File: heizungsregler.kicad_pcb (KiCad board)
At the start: 2 copper layers, 65 x 30 mm, 46 parts, among them J101 RPi_GPIO, J201 SI-52008-F, U201 ENC28J60x-SS, U202 TPS54231, Y201 Crystal

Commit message: Schaltplan weitergemacht, Footprints zugeordnet
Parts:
- removed C201, C202: 22P, Capacitor_SMD:C_0603_1608Metric
- removed C203, C204, C205, C206, C208, C212: 100N, Capacitor_SMD:C_0603_1608Metric
- removed C207, C213, C215: 10U, Capacitor_SMD:C_1210_3225Metric
- removed C209: 8N2, Capacitor_SMD:C_0603_1608Metric
- removed C210: 82P, Capacitor_SMD:C_0603_1608Metric
- removed C211: 4N3, Capacitor_SMD:C_0603_1608Metric
- removed C214: 47U, Capacitor_SMD:C_1210_3225Metric
- removed D201: D_Schottky, Diode_SMD:D_SOD-123
- removed FB201: Ferrite_Bead, Inductor_SMD:L_0603_1608Metric
- removed J101: RPi_GPIO, Connector_Samtec_HLE_THT:Samtec_HLE-120-02-xx-DV-TE_2x20_P2.54mm_Horizontal
- removed J201: SI-52008-F, kicadlibs:RJ45_BEL_STEWART_SI-52008-F
- removed L201: 22U, Inductor_SMD:L_Bourns_SRN6045TA
- removed R201, R202, R203, R204, R205, R206, R211: 0R00, Resistor_SMD:R_0603_1608Metric
- removed R207, R208, R209, R210: 49R9, Resistor_SMD:R_0603_1608Metric
- removed R212, R213: 220R, Resistor_SMD:R_0603_1608Metric
- removed R214: 2K32, Resistor_SMD:R_0603_1608Metric
- removed R215: 19K6, Resistor_SMD:R_0603_1608Metric
- removed R216: 18K7, Resistor_SMD:R_0603_1608Metric
- removed R217: 169K, Resistor_SMD:R_0603_1608Metric
- removed R218: 10K2, Resistor_SMD:R_0603_1608Metric
- removed R219: 1K96, Resistor_SMD:R_0603_1608Metric
- removed U201: ENC28J60x-SS, Package_SO:SSOP-28_5.3x10.2mm_P0.65mm
- removed U202: TPS54231, Package_SO:SOIC-8_3.9x4.9mm_P1.27mm
- removed Y201: Crystal, Crystal:Crystal_SMD_HC49-SD
- added C301: 22U, Capacitor_SMD:C_1210_3225Metric, F.Cu at (127.6, 38.6)
- added C302: 330P, Capacitor_SMD:C_0603_1608Metric, F.Cu at (135.8, 41.3)
- added C303: 47U, Capacitor_SMD:C_1210_3225Metric, F.Cu at (122.5, 44.2)
- added C304: 47U, Capacitor_SMD:C_1210_3225Metric, F.Cu at (133.4, 32.4)
- added D301: D_Schottky, Diode_SMD:D_SOD-123, F.Cu at (115.0, 44.7)
- added F301: Fuse, Fuse:Fuse_1812_4532Metric, F.Cu at (128.1, 32.8)
- added J102: Conn_01x03_Male, Connector_PinHeader_2.54mm:PinHeader_1x03_P2.54mm_Vertical, F.Cu at (89.2, 32.6)
- added J103: Conn_01x10_Male, Connector_PinHeader_2.54mm:PinHeader_1x10_P2.54mm_Vertical, F.Cu at (85.6, 32.6)
- added J301: Conn_01x02_Male, Connector_PinHeader_2.54mm:PinHeader_1x02_P2.54mm_Vertical, F.Cu at (123.3, 32.6)
- added L301: 150U, Inductor_SMD:L_Bourns-SRN4018, F.Cu at (122.7, 40.3)
- added L302: 1U, Inductor_SMD:L_1206_3216Metric, F.Cu at (127.5, 35.9)
- added Q301: BC847, Package_TO_SOT_SMD:SOT-23, F.Cu at (137.4, 32.6)
- added Q302: BC847, Package_TO_SOT_SMD:SOT-23, F.Cu at (132.8, 35.8)
- added Q303: BCP51, Package_TO_SOT_SMD:SOT-223, F.Cu at (117.1, 34.4)
- added R101: R, Resistor_SMD:R_0603_1608Metric, F.Cu at (57.2, 59.6)
- added R102: R, Resistor_SMD:R_0603_1608Metric, F.Cu at (85.3, 58.1)
- added R301: 0R00, Resistor_SMD:R_0603_1608Metric, F.Cu at (135.8, 39.8)
- added R302: 0R00, Resistor_SMD:R_0603_1608Metric, F.Cu at (129.3, 44.0)
- added R303: 1K, Resistor_SMD:R_0603_1608Metric, F.Cu at (132.8, 39.8)
- added R304: 1K, Resistor_SMD:R_0603_1608Metric, F.Cu at (136.1, 36.6)
- added R305: 0R47, Resistor_SMD:R_0603_1608Metric, F.Cu at (134.4, 38.3)
- added R306: 180, Resistor_SMD:R_0603_1608Metric, F.Cu at (126.3, 44.9)
- added R307: 4k7, Resistor_SMD:R_0603_1608Metric, F.Cu at (129.3, 42.5)
- added R308: 39K, Resistor_SMD:R_0603_1608Metric, F.Cu at (136.1, 35.1)
- added R309: 22K, Resistor_SMD:R_0603_1608Metric, F.Cu at (129.8, 41.0)
- added R310: 100K, Resistor_SMD:R_0603_1608Metric, F.Cu at (131.4, 38.3)
- added R311: 33K, Resistor_SMD:R_0603_1608Metric, F.Cu at (126.3, 43.4)
- added R312: 3K3, Resistor_SMD:R_0603_1608Metric, F.Cu at (126.8, 41.0)
- added R313: 22K, Resistor_SMD:R_0603_1608Metric, F.Cu at (132.8, 41.3)
- added R314: 220K, Resistor_SMD:R_0603_1608Metric, F.Cu at (137.4, 38.1)
- added R315: 82R, Resistor_SMD:R_0603_1608Metric, F.Cu at (132.3, 42.8)
- added U101: oled_0.96, kicadlibs:oled_0.96, F.Cu at (129.0, 114.1)
- added U301: MC34063AD, Package_SO:SOIC-8_3.9x4.9mm_P1.27mm, F.Cu at (116.4, 40.8)

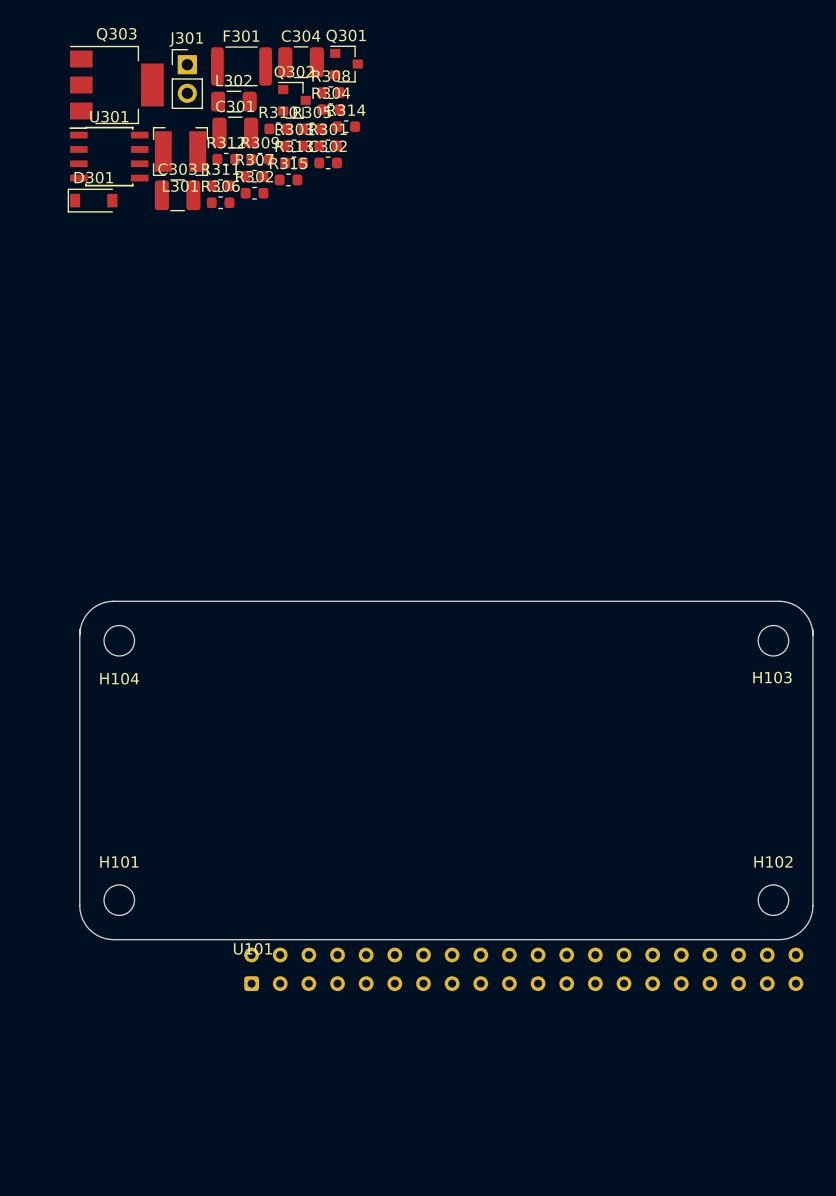
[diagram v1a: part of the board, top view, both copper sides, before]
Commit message: Platzierung begonnen, Signalnamen ENC korrigiert
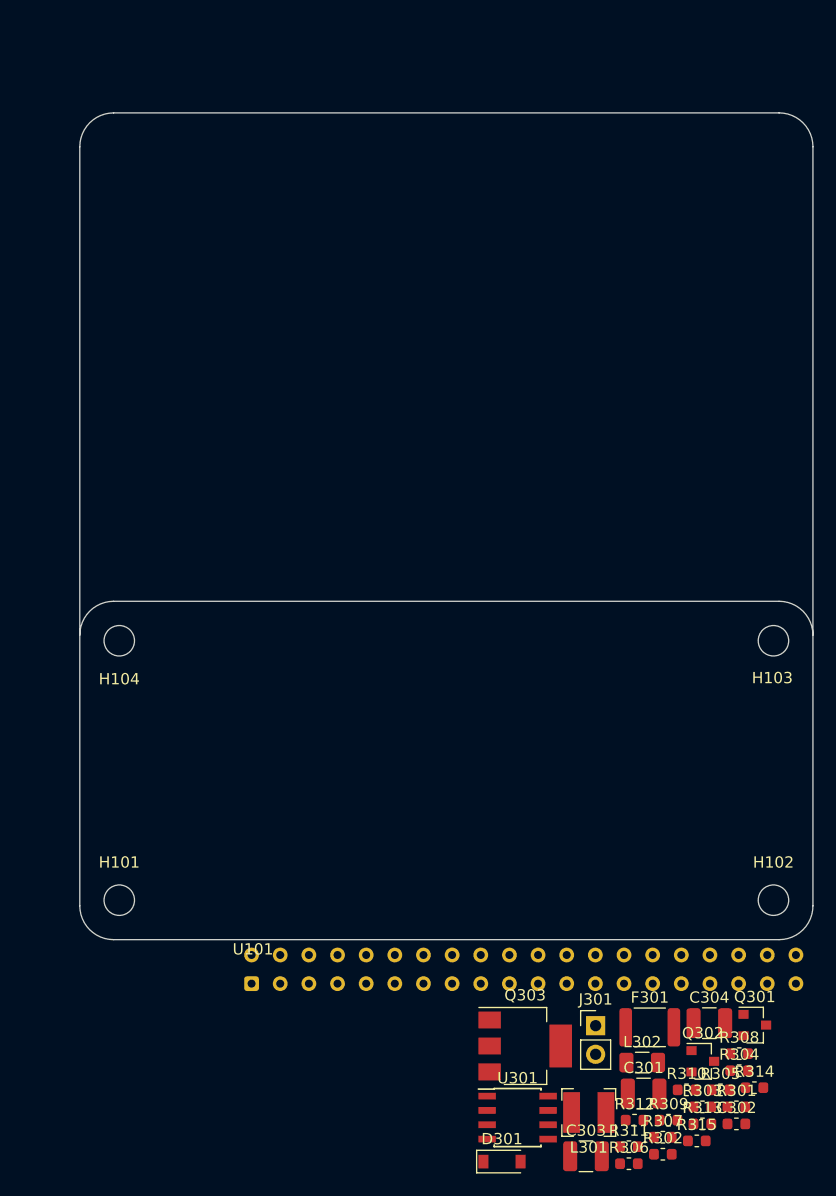
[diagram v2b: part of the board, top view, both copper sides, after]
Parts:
- moved C304 92.6 mm to (169.6, 117.6)
- moved F301 92.6 mm to (164.3, 118.0)
- moved Q301 92.6 mm to (173.6, 117.8)
- moved R301 92.6 mm to (172.0, 125.0)
- moved R308 92.6 mm to (172.3, 120.3)
- moved R311 92.6 mm to (162.5, 128.6)
- moved R314 92.6 mm to (173.6, 123.3)
- moved C302 92.6 mm to (172.0, 126.5)
- moved C303 92.6 mm to (158.7, 129.4)
- moved D301 92.6 mm to (151.2, 129.9)
- moved R304 92.6 mm to (172.3, 121.8)
- moved R306 92.6 mm to (162.5, 130.1)
- moved R312 92.6 mm to (163.0, 126.2)
- moved R315 92.6 mm to (168.5, 128.0)
- moved J301 92.6 mm to (159.5, 117.8)
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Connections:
- net /EN_#CS renamed /ENC_#CS
- net /EN_#INT renamed /ENC_#INT
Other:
- board size 65 x 30 mm -> 65 x 73.3 mm

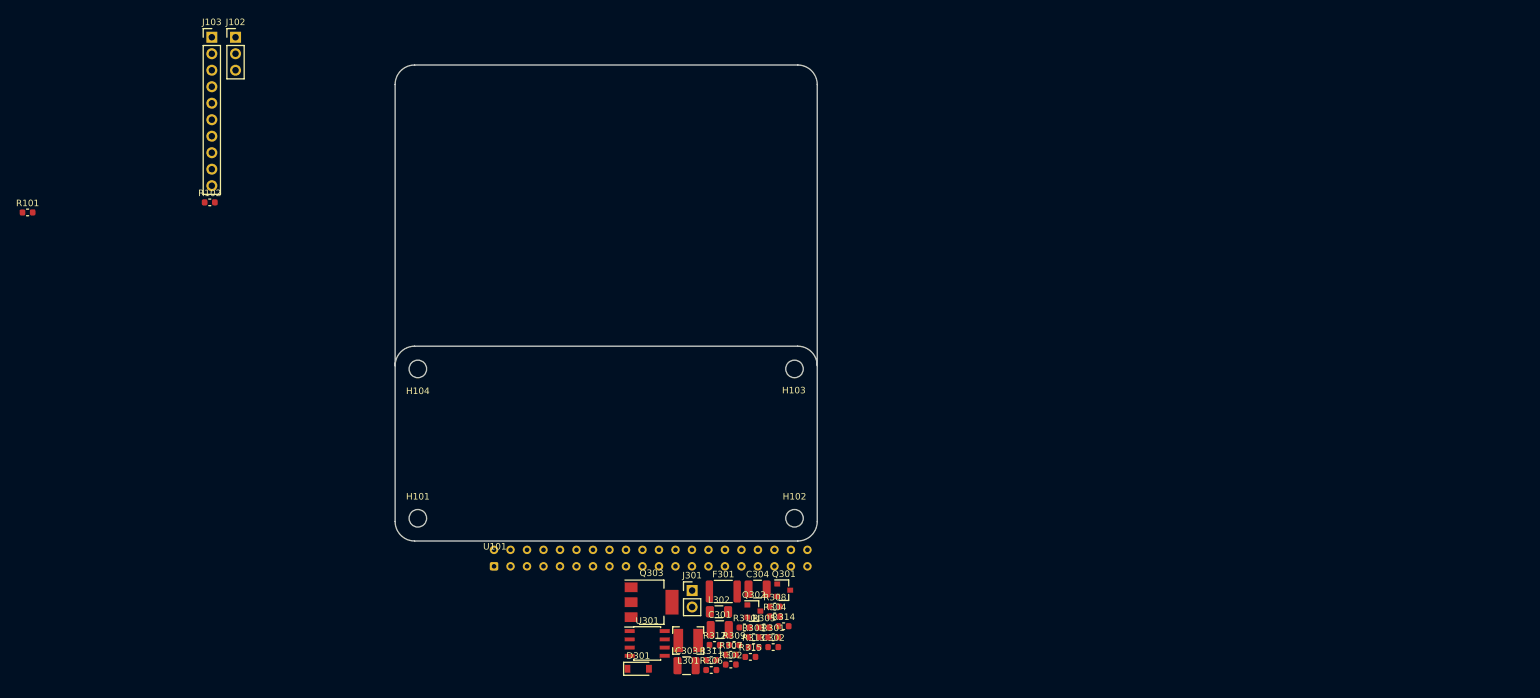
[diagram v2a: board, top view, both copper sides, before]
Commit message: ENC28J60 platziert und geroutet
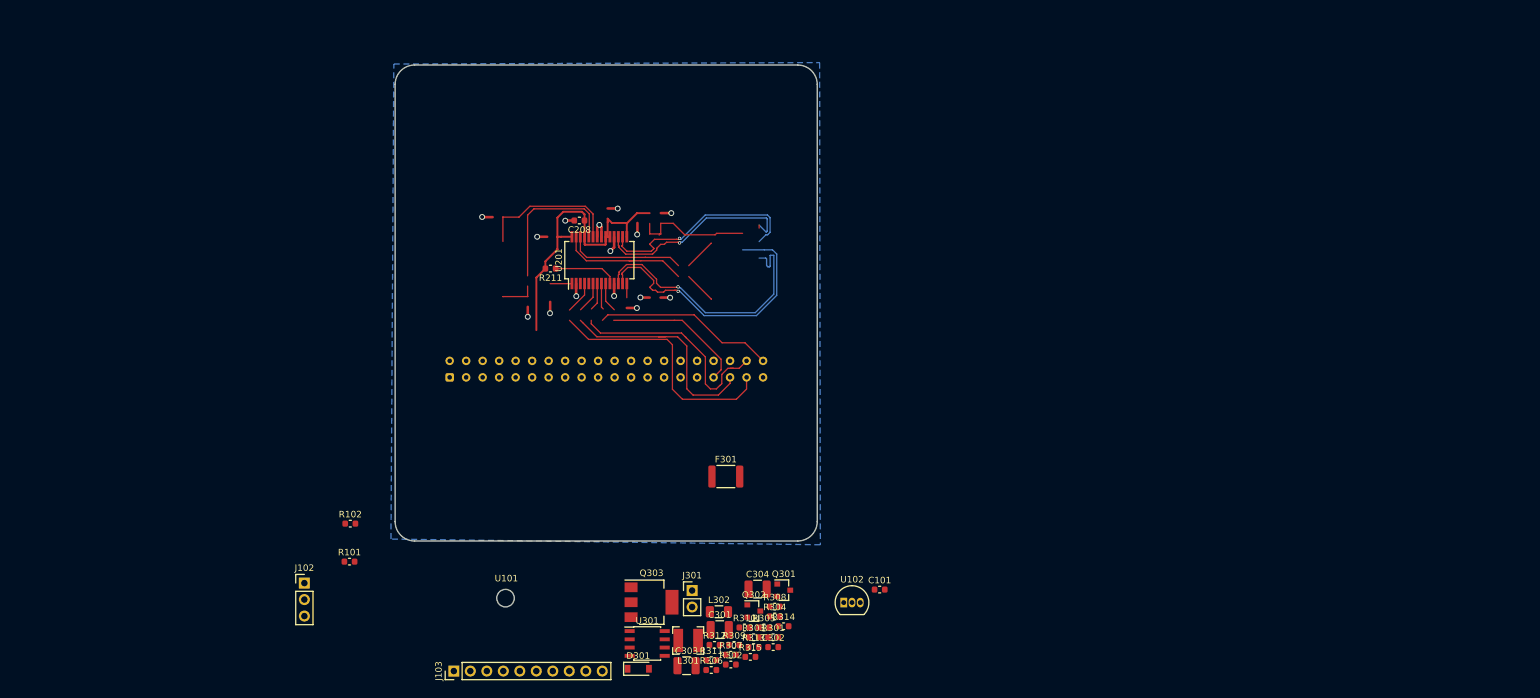
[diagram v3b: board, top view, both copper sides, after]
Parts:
- removed H101, H102, H103, H104: MountingHole, MountingHole:MountingHole_2.7mm_M2.5_DIN965
- added C101: C, Capacitor_SMD:C_0603_1608Metric, F.Cu at (188.4, 117.7)
- added C208: 100N, Capacitor_SMD:C_0603_1608Metric, F.Cu at (142.2, 60.9)
- added J101: RPi_GPIO, Connector_Samtec_HLE_THT:Samtec_HLE-120-02-xx-DV-TE_2x20_P2.54mm_Horizontal, B.Cu at (122.2, 85.0)
- added R211: 0R00, Resistor_SMD:R_0603_1608Metric, F.Cu at (137.7, 68.2)
- added U102: DS18B20, Package_TO_SOT_THT:TO-92_Inline, F.Cu at (182.9, 119.7)
- added U201: ENC28J60x-SS, Package_SO:SSOP-28_5.3x10.2mm_P0.65mm, F.Cu at (145.2, 67.0)
- F301: value Fuse -> Fuse 2A
- moved J103 104.5 mm to (122.8, 130.2), turned to 90 degrees
- moved J102 84.7 mm to (99.8, 116.7)
- moved R101 73.1 mm to (106.8, 113.4)
- moved R102 54.0 mm to (106.9, 107.5)
- moved F301 17.7 mm to (164.7, 100.3)
- moved U101 5.21 mm to (130.8, 119.0)
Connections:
- U101 pad 1: +3V3 -> (no net)
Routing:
- net +3V3: track 0.00 -> 48.0 mm
- net /Ethernet/TPIN+: track 0.00 -> 43.9 mm, vias 0 -> 1
- net /Ethernet/TPIN-: track 0.00 -> 41.9 mm, vias 0 -> 1
- net /ENC_#INT: track 0.00 -> 38.8 mm
- net /ENC_SO: track 0.00 -> 34.4 mm
- net /ENC_SI: track 0.00 -> 34.4 mm
- net /Ethernet/TPOUT-: track 0.00 -> 33.1 mm, vias 0 -> 1
- net /Ethernet/TPOUT+: track 0.00 -> 31.6 mm, vias 0 -> 1
- net /ENC_SCK: track 0.00 -> 28.0 mm
- net GND: track 0.00 -> 27.5 mm, vias 0 -> 15
- net Net-(R206-Pad1): track 0.00 -> 23.1 mm
- net Net-(C201-Pad1): track 0.00 -> 22.3 mm
- net /ENC_#CS: track 0.00 -> 22.3 mm
- net /Ethernet/LED_A: track 0.00 -> 20.0 mm
- net Net-(C203-Pad1): track 0.00 -> 18.7 mm
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- added copper zone on B.Cu, net GND
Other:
- outline, holes or cut-outs redrawn
- net class Default: trace_width 0.25 -> 0.2; via_dia 0.6 -> 0.5; via_drill 0.4 -> 0.3
- net class GND added: clearance 0.2, trace_width 0.4, via_dia 0.9, via_drill 0.6
- net class PWR added: clearance 0.2, trace_width 0.3, via_dia 0.5, via_drill 0.3
- rule trace_min: 0.01 -> 0.2
- rule via_min_size: 0.4 -> 0.5

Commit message: Noch mehr Layout
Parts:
- removed J101: RPi_GPIO, Connector_Samtec_HLE_THT:Samtec_HLE-120-02-xx-DV-TE_2x20_P2.54mm_Horizontal
- removed R102: R, Resistor_SMD:R_0603_1608Metric
- added C201: 22P, Capacitor_SMD:C_0603_1608Metric, F.Cu at (129.7, 57.2)
- added C202: 22P, Capacitor_SMD:C_0603_1608Metric, F.Cu at (134.3, 70.2)
- added C203: 100N, Capacitor_SMD:C_0603_1608Metric, F.Cu at (154.8, 57.3)
- added C204: 100N, Capacitor_SMD:C_0603_1608Metric, F.Cu at (146.9, 57.0)
- added C205: 100N, Capacitor_SMD:C_0603_1608Metric, F.Cu at (138.1, 60.2)
- added C206: 100N, Capacitor_SMD:C_0603_1608Metric, F.Cu at (150.4, 58.1)
- added C207: 10U, Capacitor_SMD:C_1210_3225Metric, F.Cu at (137.7, 68.8)
- added C209: 8N2, Capacitor_SMD:C_0603_1608Metric, F.Cu at (219.9, 47.9)
- added C210: 82P, Capacitor_SMD:C_0603_1608Metric, F.Cu at (204.4, 62.9)
- added C211: 4N3, Capacitor_SMD:C_0603_1608Metric, F.Cu at (214.6, 53.1)
- added C212: 100N, Capacitor_SMD:C_0603_1608Metric, F.Cu at (214.6, 51.6)
- added C213: 10U, Capacitor_SMD:C_1210_3225Metric, F.Cu at (207.7, 53.5)
- added C214: 47U, Capacitor_SMD:C_1210_3225Metric, F.Cu at (198.2, 68.8)
- added C215: 10U, Capacitor_SMD:C_1210_3225Metric, F.Cu at (199.4, 74.6)
- added D201: D_Schottky, Diode_SMD:D_SOD-123, F.Cu at (207.8, 50.7)
- added FB201: Ferrite_Bead, Inductor_SMD:L_0603_1608Metric, F.Cu at (153.1, 57.3)
- added H101: MountingHole, MountingHole:MountingHole_2.7mm_M2.5_DIN965, F.Cu at (117.3, 106.7)
- added H102: MountingHole, MountingHole:MountingHole_2.7mm_M2.5_DIN965, F.Cu at (175.3, 106.7)
- added H103: MountingHole, MountingHole:MountingHole_2.7mm_M2.5_DIN965, F.Cu at (175.3, 83.7)
- added H104: MountingHole, MountingHole:MountingHole_2.7mm_M2.5_DIN965, F.Cu at (117.3, 83.7)
- added L201: 22U, Inductor_SMD:L_Bourns_SRN6045TA, F.Cu at (193.1, 81.7)
- added R201: 0R00, Resistor_SMD:R_0603_1608Metric, F.Cu at (144.1, 72.3)
- added R202: 0R00, Resistor_SMD:R_0603_1608Metric, F.Cu at (142.4, 72.3)
- added R203: 0R00, Resistor_SMD:R_0603_1608Metric, F.Cu at (145.8, 72.3)
- added R204: 0R00, Resistor_SMD:R_0603_1608Metric, F.Cu at (147.5, 72.3)
- added R205: 0R00, Resistor_SMD:R_0603_1608Metric, F.Cu at (140.7, 72.3)
- added R206: 0R00, Resistor_SMD:R_0603_1608Metric, F.Cu at (134.2, 67.0)
- added R207: 49R9, Resistor_SMD:R_0603_1608Metric, F.Cu at (154.8, 60.6)
- added R208: 49R9, Resistor_SMD:R_0603_1608Metric, F.Cu at (153.1, 68.8)
- added R209: 49R9, Resistor_SMD:R_0603_1608Metric, F.Cu at (153.1, 60.5)
- added R210: 49R9, Resistor_SMD:R_0603_1608Metric, F.Cu at (154.7, 68.8)
- added R212: 220R, Resistor_SMD:R_0603_1608Metric, F.Cu at (158.3, 64.6)
- added R213: 220R, Resistor_SMD:R_0603_1608Metric, F.Cu at (158.3, 66.3)
- added R214: 2K32, Resistor_SMD:R_0603_1608Metric, F.Cu at (149.5, 70.4)
- added R215: 19K6, Resistor_SMD:R_0603_1608Metric, F.Cu at (221.5, 46.2)
- added R216: 18K7, Resistor_SMD:R_0603_1608Metric, F.Cu at (217.7, 49.4)
- added R217: 169K, Resistor_SMD:R_0603_1608Metric, F.Cu at (194.3, 70.6)
- added R218: 10K2, Resistor_SMD:R_0603_1608Metric, F.Cu at (214.7, 50.1)
- added R219: 1K96, Resistor_SMD:R_0603_1608Metric, F.Cu at (209.9, 55.9)
- added U202: TPS54231, Package_SO:SOIC-8_3.9x4.9mm_P1.27mm, F.Cu at (211.6, 46.6)
- added Y201: Crystal, Crystal:Crystal_SMD_HC49-SD, F.Cu at (130.4, 65.2)
- moved U102 83.9 mm to (117.1, 67.6), turned to 270 degrees
- moved C101 83.8 mm to (117.1, 73.6), turned to 270 degrees
- moved U101 65.8 mm to (135.1, 53.3)
- moved J102 27.9 mm to (127.6, 113.8), turned to 270 degrees
- moved J103 19.6 mm to (133.5, 113.8)
- moved R101 17.3 mm to (123.7, 109.4), turned to 180 degrees
- moved C304 6.16 mm to (164.5, 114.1)
- moved Q301 6.00 mm to (168.8, 114.2)
- moved C208 3.16 mm to (142.2, 57.7)
- moved U201 3.16 mm to (145.3, 63.8)
- moved R211 3.16 mm to (137.8, 65.1)
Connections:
- U101 pad 1: (no net) -> +3V3
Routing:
- net +3V3: track 48.0 -> 156.2 mm
- net /DQ: track 0.00 -> 58.8 mm
- net /REL2: track 0.00 -> 53.0 mm
- net /REL1: track 0.00 -> 52.8 mm
- net /SCL: track 0.00 -> 51.0 mm
- net /SDA: track 0.00 -> 44.0 mm
- net /Ethernet/TPIN-: track 41.9 -> 35.2 mm
- net /Ethernet/TPIN+: track 43.9 -> 37.9 mm
- net Net-(C203-Pad1): track 18.7 -> 24.7 mm
- net Net-(J201-PadAG): track 4.92 -> 8.35 mm
- net +5V: track 0.00 -> 2.54 mm
- net /ENC_#INT: track 38.8 -> 40.7 mm
- net /ENC_SI: track 34.4 -> 36.2 mm
- net GND: track 27.5 -> 29.3 mm, vias 15 -> 16
- net /ENC_#CS: track 22.3 -> 24.0 mm
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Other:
- board size 65 x 73.3 mm -> 65 x 65.3 mm
